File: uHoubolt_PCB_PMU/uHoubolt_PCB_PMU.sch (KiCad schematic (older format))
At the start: 46 parts, among them J1 Conn_01x04, J2 Conn_01x02, J3 Conn_01x04_MountingPin, J4 Conn_01x02, Q1 ZXMN3F30FH, Q2 Si7141DP, SW1 SW_Push_SPDT, SW2 SW_Push_SPDT, U1 INA226, U2 MAX1873SEEE

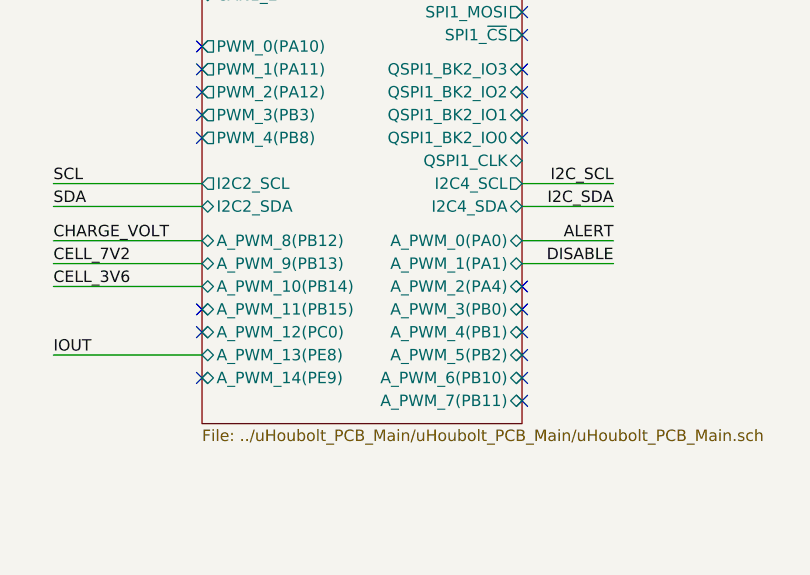
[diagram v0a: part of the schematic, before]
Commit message: solve ERC errors
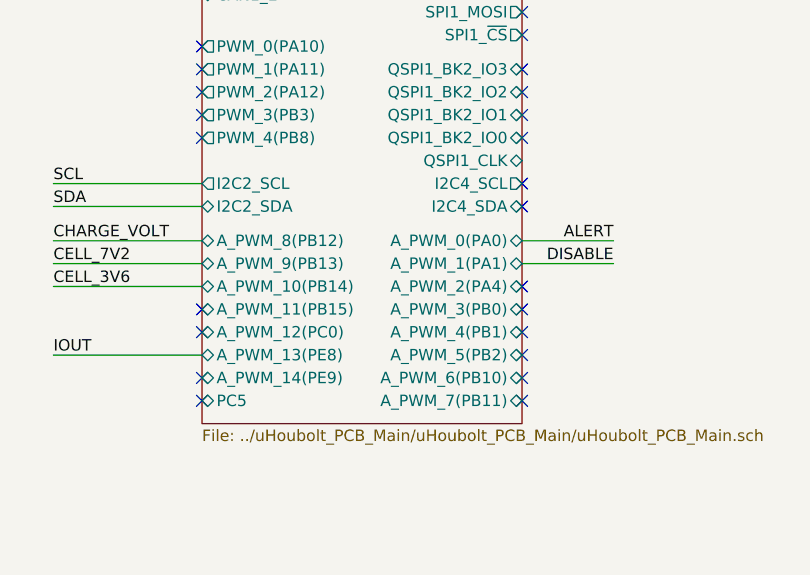
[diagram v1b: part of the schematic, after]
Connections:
- no-connect marks 29 -> 32
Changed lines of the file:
@@
 Wire Wire Line
 	825  6200 1475 6200
-Text Label 3275 5750 2    50   ~ 0
-I2C_SCL
-Wire Wire Line
-	2875 5750 3275 5750
-Text Label 3275 5850 2    50   ~ 0
-I2C_SDA
-Wire Wire Line
-	2875 5850 3275 5850
 $Comp
 L Analog_ADC:INA226 U1
@@
 F39 "CAN1_H" B L 1475 4825 50
 F40 "CAN1_L" B L 1475 4925 50
+F41 "PC5" B L 1475 6700 50
 $EndSheet
 Wire Wire Line
@@
 	5750 4050 6050 4050
 Connection ~ 6050 4050
+NoConn ~ 2875 5750
+NoConn ~ 2875 5850
+NoConn ~ 1475 6700
 $EndSCHEMATC

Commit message: connect power flags, update main
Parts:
- C12: footprint (none) -> Capacitor_Tantalum_SMD:CP_EIA-7343-43_Kemet-X
- C13: footprint (none) -> Capacitor_Tantalum_SMD:CP_EIA-7343-31_Kemet-D
- R1, R10, R11, R12, R13, R14, R15, R16, R17, R2, R3, R4, R46, R5, R6, R8, R9: footprint (none) -> Resistor_SMD:R_0603_1608Metric
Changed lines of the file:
@@
 F 0 "R16" V 8996 3400 50  0000 C CNN
 F 1 "4.7" V 8905 3400 50  0000 C CNN
-F 2 "" H 8800 3400 50  0001 C CNN
+F 2 "Resistor_SMD:R_0603_1608Metric" H 8800 3400 50  0001 C CNN
 F 3 "~" H 8800 3400 50  0001 C CNN
 	1    8800 3400
@@
 F 0 "R17" V 9200 3650 50  0000 C CNN
 F 1 "4.7" V 9105 3650 50  0000 C CNN
-F 2 "" H 9000 3650 50  0001 C CNN
+F 2 "Resistor_SMD:R_0603_1608Metric" H 9000 3650 50  0001 C CNN
 F 3 "~" H 9000 3650 50  0001 C CNN
 	1    9000 3650
@@
 F 0 "R10" H 6800 3900 50  0000 L CNN
 F 1 "100k" H 6750 3800 50  0000 L CNN
-F 2 "" H 6700 3900 50  0001 C CNN
+F 2 "Resistor_SMD:R_0603_1608Metric" H 6700 3900 50  0001 C CNN
 F 3 "~" H 6700 3900 50  0001 C CNN
 	1    6700 3900
@@
 F 0 "R9" H 6309 3846 50  0000 L CNN
 F 1 "100k" H 6309 3755 50  0000 L CNN
-F 2 "" H 6250 3800 50  0001 C CNN
+F 2 "Resistor_SMD:R_0603_1608Metric" H 6250 3800 50  0001 C CNN
 F 3 "~" H 6250 3800 50  0001 C CNN
 	1    6250 3800
@@
 F 0 "R11" H 6759 4646 50  0000 L CNN
 F 1 "100k" H 6759 4555 50  0000 L CNN
-F 2 "" H 6700 4600 50  0001 C CNN
+F 2 "Resistor_SMD:R_0603_1608Metric" H 6700 4600 50  0001 C CNN
 F 3 "~" H 6700 4600 50  0001 C CNN
 	1    6700 4600
@@
 F 0 "C12" H 9765 3846 50  0000 L CNN
 F 1 "47u" H 9765 3755 50  0000 L CNN
-F 2 "" H 9650 3800 50  0001 C CNN
-F 3 "~" H 9650 3800 50  0001 C CNN
+F 2 "Capacitor_Tantalum_SMD:CP_EIA-7343-43_Kemet-X" H 9650 3800 50  0001 C CNN
+F 3 "https://www.mouser.at/ProductDetail/KEMET/T498X476K035ATE500/?qs=AXRVZpzixL9KYfK2Sw922Q%3D%3D" H 9650 3800 50  0001 C CNN
 	1    9650 3800
 	1    0    0    -1
@@
 F 0 "C13" H 10300 4700 50  0000 L CNN
 F 1 "68uF" H 10250 4600 50  0000 L CNN
-F 2 "" H 10150 4800 50  0001 C CNN
-F 3 "~" H 10150 4800 50  0001 C CNN
+F 2 "Capacitor_Tantalum_SMD:CP_EIA-7343-31_Kemet-D" H 10150 4800 50  0001 C CNN
+F 3 "https://www.mouser.at/ProductDetail/KEMET/T495D686K020ATE300/?qs=qKZkgl8zrZGJQw%2F5Tjohww%3D%3D" H 10150 4800 50  0001 C CNN
 	1    10150 4800
 	1    0    0    -1
@@
 F 0 "R15" V 8350 5525 50  0000 L CNN
 F 1 "10k" V 8450 5525 50  0000 L CNN
-F 2 "" H 8550 5575 50  0001 C CNN
+F 2 "Resistor_SMD:R_0603_1608Metric" H 8550 5575 50  0001 C CNN
 F 3 "~" H 8550 5575 50  0001 C CNN
 	1    8550 5575
@@
 	1    0    0    -1
 $EndComp
-Wire Wire Line
-	6550 3400 6750 3400
 $Sheet
 S 8600 1050 850  750
@@
 F1 "balancer.sch" 50
 F2 "GND_OUT" I R 9450 1725 50
+F3 "BATT_GND" I L 8600 1600 50
+F4 "BATT_VCC" I L 8600 1150 50
+F5 "BATT7V2" I L 8600 1450 50
+F6 "BATT3V6" I L 8600 1300 50
 $EndSheet
 $Comp
@@
 F 0 "R5" H 2884 2996 50  0000 L CNN
 F 1 "10k" H 2884 2905 50  0000 L CNN
-F 2 "" H 2825 2950 50  0001 C CNN
+F 2 "Resistor_SMD:R_0603_1608Metric" H 2825 2950 50  0001 C CNN
 F 3 "~" H 2825 2950 50  0001 C CNN
 	1    2825 2950
@@
 F 0 "R6" H 2884 3296 50  0000 L CNN
 F 1 "1k" H 2884 3205 50  0000 L CNN
-F 2 "" H 2825 3250 50  0001 C CNN
+F 2 "Resistor_SMD:R_0603_1608Metric" H 2825 3250 50  0001 C CNN
 F 3 "~" H 2825 3250 50  0001 C CNN
 	1    2825 3250
@@
 F 0 "R3" H 1984 2996 50  0000 L CNN
 F 1 "500" H 1984 2905 50  0000 L CNN
-F 2 "" H 1925 2950 50  0001 C CNN
+F 2 "Resistor_SMD:R_0603_1608Metric" H 1925 2950 50  0001 C CNN
 F 3 "~" H 1925 2950 50  0001 C CNN
 	1    1925 2950
@@
 F 0 "R4" H 1984 3296 50  0000 L CNN
 F 1 "1k" H 1984 3205 50  0000 L CNN
-F 2 "" H 1925 3250 50  0001 C CNN
+F 2 "Resistor_SMD:R_0603_1608Metric" H 1925 3250 50  0001 C CNN
 F 3 "~" H 1925 3250 50  0001 C CNN
 	1    1925 3250
@@
 F 0 "R1" H 1309 2996 50  0000 L CNN
 F 1 "3k" H 1309 2905 50  0000 L CNN
-F 2 "" H 1250 2950 50  0001 C CNN
+F 2 "Resistor_SMD:R_0603_1608Metric" H 1250 2950 50  0001 C CNN
 F 3 "~" H 1250 2950 50  0001 C CNN
 	1    1250 2950
@@
 F 0 "R2" H 1309 3296 50  0000 L CNN
 F 1 "1k5" H 1309 3205 50  0000 L CNN
-F 2 "" H 1250 3250 50  0001 C CNN
+F 2 "Resistor_SMD:R_0603_1608Metric" H 1250 3250 50  0001 C CNN
 F 3 "~" H 1250 3250 50  0001 C CNN
 	1    1250 3250
@@
 Wire Wire Line
 	1250 2450 1250 2850
-Text HLabel 8600 1150 2    50   Output ~ 0
-BATT_VCC
-Text HLabel 8600 1300 2    50   Output ~ 0
-BATT3V6
-Text HLabel 8600 1450 2    50   Output ~ 0
-BATT7V2
-Text HLabel 8600 1600 2    50   Output ~ 0
-BATT_GND
 Text Label 8200 1150 0    50   ~ 0
 BATT_VCC
@@
 F 0 "R12" H 6859 1346 50  0000 L CNN
 F 1 "2.7k" H 6859 1255 50  0000 L CNN
-F 2 "" H 6800 1300 50  0001 C CNN
+F 2 "Resistor_SMD:R_0603_1608Metric" H 6800 1300 50  0001 C CNN
 F 3 "~" H 6800 1300 50  0001 C CNN
 	1    6800 1300
@@
 F 0 "R13" H 7209 1346 50  0000 L CNN
 F 1 "2.7k" H 7209 1255 50  0000 L CNN
-F 2 "" H 7150 1300 50  0001 C CNN
+F 2 "Resistor_SMD:R_0603_1608Metric" H 7150 1300 50  0001 C CNN
 F 3 "~" H 7150 1300 50  0001 C CNN
 	1    7150 1300
@@
 F 0 "R14" H 7559 1346 50  0000 L CNN
 F 1 "2.7k" H 7559 1255 50  0000 L CNN
-F 2 "" H 7500 1300 50  0001 C CNN
+F 2 "Resistor_SMD:R_0603_1608Metric" H 7500 1300 50  0001 C CNN
 F 3 "~" H 7500 1300 50  0001 C CNN
 	1    7500 1300
@@
 F 0 "R8" V 5625 3800 50  0000 L CNN
 F 1 "200" V 5700 3775 50  0000 L CNN
-F 2 "" H 5550 3850 50  0001 C CNN
+F 2 "Resistor_SMD:R_0603_1608Metric" H 5550 3850 50  0001 C CNN
 F 3 "~" H 5550 3850 50  0001 C CNN
 	1    5550 3850
@@
 F 0 "R46" H 5809 3996 50  0000 L CNN
 F 1 "10k" H 5809 3905 50  0000 L CNN
-F 2 "" H 5750 3950 50  0001 C CNN
+F 2 "Resistor_SMD:R_0603_1608Metric" H 5750 3950 50  0001 C CNN
 F 3 "~" H 5750 3950 50  0001 C CNN
 	1    5750 3950
@@
 NoConn ~ 2875 5850
 NoConn ~ 1475 6700
+$Comp
+L power:PWR_FLAG #FLG0101
+U 1 1 600495A4
+P 2825 2750
+F 0 "#FLG0101" H 2825 2825 50  0001 C CNN
+F 1 "PWR_FLAG" V 2825 2878 50  0000 L CNN
+F 2 "" H 2825 2750 50  0001 C CNN
+F 3 "~" H 2825 2750 50  0001 C CNN
+	1    2825 2750
+	0    1    1    0
+$EndComp
+Connection ~ 2825 2750
+$Comp
+L power:PWR_FLAG #FLG0102
+U 1 1 6004D134
+P 4850 2075
+F 0 "#FLG0102" H 4850 2150 50  0001 C CNN
+F 1 "PWR_FLAG" V 4850 2203 50  0000 L CNN
+F 2 "" H 4850 2075 50  0001 C CNN
+F 3 "~" H 4850 2075 50  0001 C CNN
+	1    4850 2075
+	0    1    1    0
+$EndComp
+Connection ~ 4850 2075
+Wire Wire Line
+	6550 3400 6750 3400
 $EndSCHEMATC

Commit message: add mosfet in schematic, draw outer bounds of pcb
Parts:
- removed SW2: SW_Push_SPDT, symbol Switch:SW_Push_SPDT
- added Q5: 2N3904, Package_TO_SOT_THT:TO-92_Inline, symbol Transistor_BJT:2N3904
- added Q6: Si7141DP, Package_SO:PowerPAK_SO-8_Single, symbol Transistor_FET:Si7141DP
- added R47, R48: 1k, Resistor_SMD:R_0603_1608Metric, symbol Device:R_Small
- D1, D2: footprint (none) -> Diode_SMD:D_2114_3652Metric
- J1: footprint (none) -> Connector_Molex:Molex_PicoBlade_53048-0410_1x04_P1.25mm_Horizontal
- J2: footprint (none) -> Connector_Molex:Molex_PicoBlade_53047-0210_1x02_P1.25mm_Vertical
- J3: footprint (none) -> Connector_JST:JST_GH_SM04B-GHS-TB_1x04-1MP_P1.25mm_Horizontal
- J4: footprint (none) -> Connector_Molex:Molex_PicoBlade_53048-0210_1x02_P1.25mm_Horizontal
- L1: footprint (none) -> Inductor_SMD:L_Vishay_IHLP-2525
- SW1: footprint (none) -> TXV_LIB:MicroSwitch
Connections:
- wire segments 154 -> 165
- no-connect marks 32 -> 31
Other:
- moved on the sheet: C1, C10, C11, C12, C13, C2, C3, C4, C5, C6, C7, C8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

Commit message: add ignition bus, placement 75% done
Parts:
- removed Q5: 2N3904, Package_TO_SOT_THT:TO-92_Inline, symbol Transistor_BJT:2N3904
- added C47: 100n, Capacitor_SMD:C_0402_1005Metric, symbol Device:C_Small
- added J10: Conn_01x02, Connector_Molex:Molex_Micro-Fit_3.0_43650-0215_1x02_P3.00mm_Vertical, symbol Connector_Generic:Conn_01x02
- added Q5, Q7: MMBT3904, Package_TO_SOT_SMD:SOT-23, symbol Transistor_BJT:MMBT3904
- added Q8: Si7141DP, Package_SO:PowerPAK_SO-8_Single, symbol Transistor_FET:Si7141DP
- added Q9: BSF030NE2LQ, Package_DirectFET:DirectFET_SQ, symbol Transistor_FET:BSF030NE2LQ
- added R49, R50, R55: 1k, Resistor_SMD:R_0603_1608Metric, symbol Device:R_Small
- added R51: 4m, symbol Device:R_Small
- added R52, R53, R54: 2.7k, Resistor_SMD:R_0603_1608Metric, symbol Device:R_Small
- added SW2: SW_Push_SPDT, TXV_LIB:MicroSwitch, symbol Switch:SW_Push_SPDT
- added U10: INA226, Package_SO:VSSOP-10_3x3mm_P0.5mm, symbol Analog_ADC:INA226
- J_BALANCE1: renamed from J1; footprint Connector_Molex:Molex_PicoBlade_53048-0410_1x04_P1.25mm_Horizontal -> Connector_JST:JST_XH_B4B-XH-AM_1x04_P2.50mm_Vertical
- J_IN1: renamed from J4; footprint Connector_Molex:Molex_PicoBlade_53048-0210_1x02_P1.25mm_Horizontal -> Connector_Molex:Molex_Mega-Fit_76829-0002_2x01_P5.70mm_Vertical
- J_OUT1: renamed from J2; footprint Connector_Molex:Molex_PicoBlade_53047-0210_1x02_P1.25mm_Vertical -> Connector_Molex:Molex_Mega-Fit_76829-0002_2x01_P5.70mm_Vertical
- J_UMBILICAL1: renamed from J3; footprint Connector_JST:JST_GH_SM04B-GHS-TB_1x04-1MP_P1.25mm_Horizontal -> Connector_Molex:Molex_MicroClasp_55932-0510_1x05_P2.00mm_Vertical
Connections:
- wire segments 165 -> 201
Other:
- note added: "Adress: 0x44\n\n"
- note added: "Ignition\n"
- moved on the sheet: C1, J_IN1, J_OUT1, Q6, R1, R12, R13, R14, R2, R3, R4, R47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

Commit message: add footprints of 2 shunts
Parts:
- R18, R19: footprint (none) -> Resistor_SMD:R_2512_6332Metric
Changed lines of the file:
@@
 F 0 "R18" V 9821 3550 50  0000 C CNN
 F 1 "0.033" V 9725 3550 50  0000 C CNN
-F 2 "" H 9625 3550 50  0001 C CNN
+F 2 "Resistor_SMD:R_2512_6332Metric" H 9625 3550 50  0001 C CNN
 F 3 "~" H 9625 3550 50  0001 C CNN
 	1    9625 3550
@@
 F 0 "R19" V 10250 4625 50  0000 L CNN
 F 1 "0.068" V 10325 4575 50  0000 L CNN
-F 2 "" H 10175 4700 50  0001 C CNN
+F 2 "Resistor_SMD:R_2512_6332Metric" H 10175 4700 50  0001 C CNN
 F 3 "~" H 10175 4700 50  0001 C CNN
 	1    10175 4700
@@
 	7875 8525 7875 8225
 $Comp
-L power:+BATT #PWR?
+L power:+BATT #PWR0111
 U 1 1 60978816
 P 6000 7425
-F 0 "#PWR?" H 6000 7275 50  0001 C CNN
+F 0 "#PWR0111" H 6000 7275 50  0001 C CNN
 F 1 "+BATT" H 6015 7598 50  0000 C CNN
 F 2 "" H 6000 7425 50  0001 C CNN
